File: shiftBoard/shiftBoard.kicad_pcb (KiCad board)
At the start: 2 copper layers, 88 x 93 mm, 37 parts, among them J1 Screw_Terminal_01x02, J10 Screw_Terminal_01x02, J11 Screw_Terminal_01x02, J12 Screw_Terminal_01x02, J2 Screw_Terminal_01x02, J3 Screw_Terminal_01x02, J4 Screw_Terminal_01x02, J5 Screw_Terminal_01x02, J6 Screw_Terminal_01x02, J7 Screw_Terminal_01x02, J8 Screw_Terminal_01x02, J9 Screw_Terminal_01x02, Q1 AO3400A, Q2 AO3400A, Q3 AO3400A, Q4 AO3400A, Q5 AO3400A, Q6 AO3400A, Q7 AO3400A, Q8 AO3400A, U2 74HC595

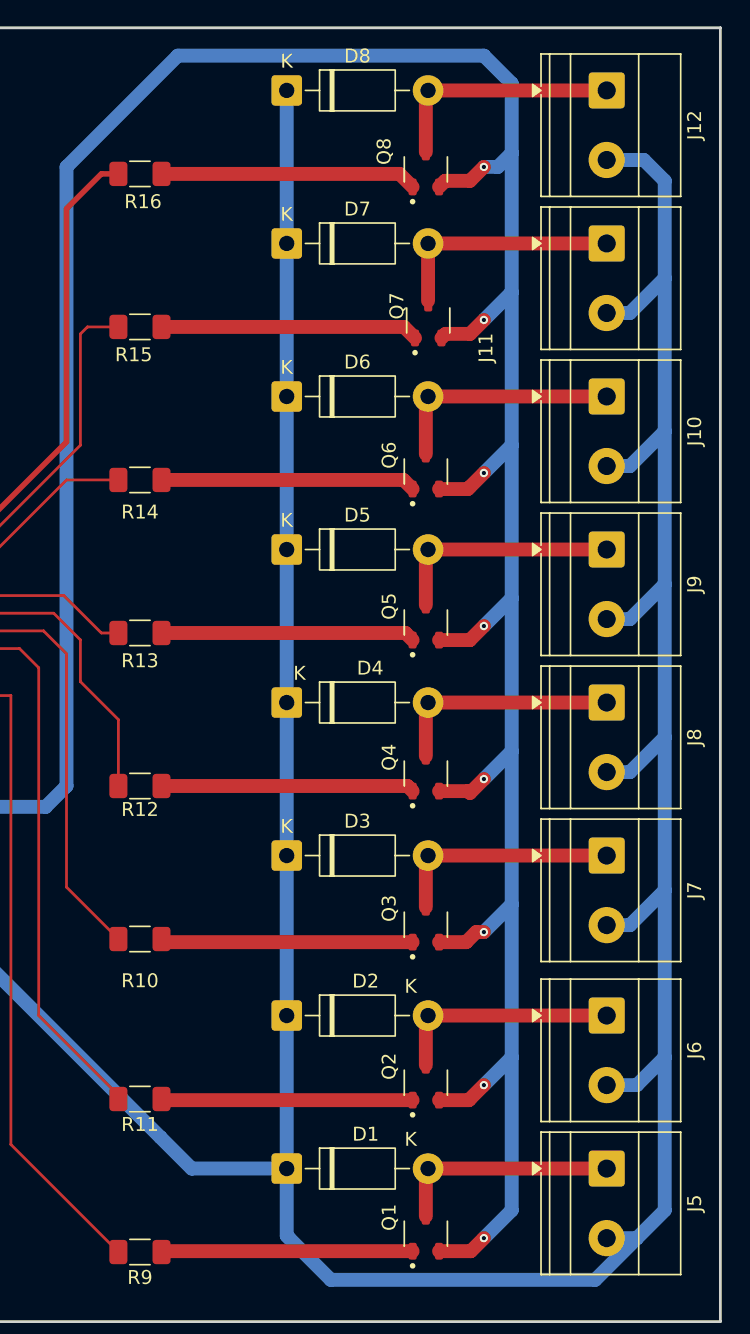
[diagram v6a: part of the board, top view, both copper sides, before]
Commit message: pcb led indicator addition
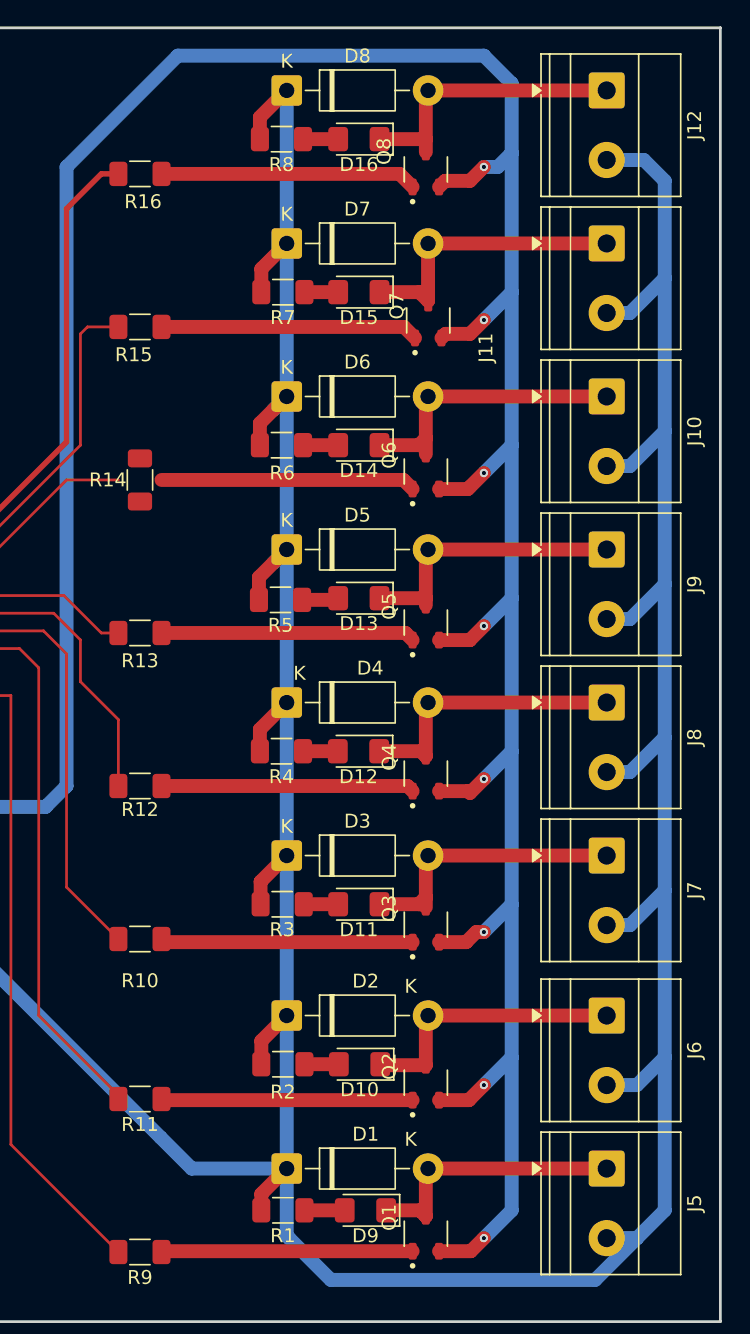
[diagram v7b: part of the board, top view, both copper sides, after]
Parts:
- added D10: LED, LED_SMD:LED_1206_3216Metric_Pad1.42x1.75mm_HandSolder, F.Cu at (224.1, 111.5)
- added D11: LED, LED_SMD:LED_1206_3216Metric_Pad1.42x1.75mm_HandSolder, F.Cu at (224.0, 100.0)
- added D12: LED, LED_SMD:LED_1206_3216Metric_Pad1.42x1.75mm_HandSolder, F.Cu at (224.0, 89.0)
- added D13: LED, LED_SMD:LED_1206_3216Metric_Pad1.42x1.75mm_HandSolder, F.Cu at (224.0, 78.0)
- added D14: LED, LED_SMD:LED_1206_3216Metric_Pad1.42x1.75mm_HandSolder, F.Cu at (224.0, 67.0)
- added D15: LED, LED_SMD:LED_1206_3216Metric_Pad1.42x1.75mm_HandSolder, F.Cu at (224.0, 56.0)
- added D16: LED, LED_SMD:LED_1206_3216Metric_Pad1.42x1.75mm_HandSolder, F.Cu at (224.0, 45.0)
- added D9: LED, LED_SMD:LED_1206_3216Metric_Pad1.42x1.75mm_HandSolder, F.Cu at (224.5, 122.0)
- added R1: 1K, Resistor_SMD:R_1206_3216Metric_Pad1.30x1.75mm_HandSolder, F.Cu at (218.6, 122.0)
- added R2: 1K, Resistor_SMD:R_1206_3216Metric_Pad1.30x1.75mm_HandSolder, F.Cu at (218.6, 111.5)
- added R3: 1K, Resistor_SMD:R_1206_3216Metric_Pad1.30x1.75mm_HandSolder, F.Cu at (218.5, 100.0)
- added R4: 1K, Resistor_SMD:R_1206_3216Metric_Pad1.30x1.75mm_HandSolder, F.Cu at (218.4, 89.0)
- added R5: 1K, Resistor_SMD:R_1206_3216Metric_Pad1.30x1.75mm_HandSolder, F.Cu at (218.4, 78.1)
- added R6: 1K, Resistor_SMD:R_1206_3216Metric_Pad1.30x1.75mm_HandSolder, F.Cu at (218.4, 67.0)
- added R7: 1K, Resistor_SMD:R_1206_3216Metric_Pad1.30x1.75mm_HandSolder, F.Cu at (218.6, 56.0)
- added R8: 1K, Resistor_SMD:R_1206_3216Metric_Pad1.30x1.75mm_HandSolder, F.Cu at (218.4, 45.0)
- turned R14 to 90 degrees
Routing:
- net /12v: track 286.0 -> 322.7 mm
- net Net-(D15-K): track 17.0 -> 20.7 mm
- net Net-(D14-K): track 17.0 -> 20.6 mm
- net Net-(D11-K): track 16.6 -> 20.2 mm
- net Net-(D12-K): track 16.8 -> 20.3 mm
- net Net-(D16-K): track 17.3 -> 20.7 mm
- net Net-(D13-K): track 16.9 -> 20.2 mm
- net Net-(D10-K): track 16.5 -> 19.8 mm
- net Net-(D1-A): track 16.3 -> 19.4 mm
- net Net-(D9-A): track 0.00 -> 2.90 mm
- net Net-(D13-A): track 0.00 -> 2.64 mm
- net Net-(D16-A): track 0.00 -> 2.53 mm
- net Net-(D14-A): track 0.00 -> 2.53 mm
- net Net-(D12-A): track 0.00 -> 2.50 mm
- net Net-(D11-A): track 0.00 -> 2.47 mm
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
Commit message: bypass capacitor
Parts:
- added C1: 100nF, Capacitor_SMD:C_1206_3216Metric_Pad1.33x1.80mm_HandSolder, F.Cu at (183.9, 58.5)
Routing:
- net /VCC: track 41.8 -> 53.1 mm
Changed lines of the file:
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@@
 		)
 	)
+	(footprint "Capacitor_SMD:C_1206_3216Metric_Pad1.33x1.80mm_HandSolder"
+		(layer "F.Cu")
+		(at 183.9375 58.5 -90)
+		(descr "Capacitor SMD 1206 (3216 Metric), square (rectangular) end terminal, IPC-7351 nominal with elongated pad for handsoldering. (Body size source: IPC-SM-782 page 76, https://www.pcb-3d.com/wordpress/wp-content/uploads/ipc-sm-782a_amendment_1_and_2.pdf), generated with kicad-footprint-generator")
+		(tags "capacitor handsolder")
+		(property "Reference" "C1"
+			(at 0 -1.85 90)
+			(layer "F.SilkS")
+			(effects
+				(font
+					(size 1 1)
+					(thickness 0.15)
+				)
+			)
+		)
+		(property "Value" "100nF"
+			(at 0 1.85 90)
+			(layer "F.Fab")
+			(effects
+				(font
+					(size 1 1)
+					(thickness 0.15)
+				)
+			)
+		)
+		(property "Datasheet" "~"
+			(at 0 0 90)
+			(layer "F.Fab")
+			(hide yes)
+			(effects
+				(font
+					(size 1.27 1.27)
+					(thickness 0.15)
+				)
+			)
+		)
+		(property "Description" "Unpolarized capacitor"
+			(at 0 0 90)
+			(layer "F.Fab")
+			(hide yes)
+			(effects
+				(font
+					(size 1.27 1.27)
+					(thickness 0.15)
+				)
+			)
+		)
+		(property ki_fp_filters "C_*")
+		(sheetname "/")
+		(sheetfile "shiftBoard.kicad_sch")
+		(attr smd)
+		(fp_line
+			(start -0.711252 0.91)
+			(end 0.711252 0.91)
+			(stroke
+				(width 0.12)
+				(type solid)
+			)
+			(layer "F.SilkS")
+		)
+		(fp_line
+			(start -0.711252 -0.91)
+			(end 0.711252 -0.91)
+			(stroke
+				(width 0.12)
+				(type solid)
+			)
+			(layer "F.SilkS")
+		)
+		(fp_rect
+			(start -2.48 -1.15)
+			(end 2.48 1.15)
+			(stroke
+				(width 0.05)
+				(type solid)
+			)
+			(fill no)
+			(layer "F.CrtYd")
+		)
+		(fp_rect
+			(start -1.6 -0.8)
+			(end 1.6 0.8)
+			(stroke
+				(width 0.1)
+				(type solid)
+			)
+			(fill no)
+			(layer "F.Fab")
+		)
+		(fp_text user "${REFERENCE}"
+			(at 0 0 90)
+			(layer "F.Fab")
+			(effects
+				(font
+					(size 0.8 0.8)
+					(thickness 0.12)
+				)
+			)
+		)
+		(pad "1" smd roundrect
+			(at -1.5625 0 270)
+			(size 1.325 1.8)
+			(layers "F.Cu" "F.Mask" "F.Paste")
+			(roundrect_rratio 0.188679)
+			(net 2 "/VCC")
+			(pintype "passive")
+		)
+		(pad "2" smd roundrect
+			(at 1.5625 0 270)
+			(size 1.325 1.8)
+			(layers "F.Cu" "F.Mask" "F.Paste")
+			(roundrect_rratio 0.188679)
+			(net 2 "/VCC")
+			(pintype "passive")
+		)
+		(embedded_fonts no)
+		(model "${KICAD9_3DMODEL_DIR}/Capacitor_SMD.3dshapes/C_1206_3216Metric.step"
+			(offset
+				(xyz 0 0 0)
+			)
+			(scale
+				(xyz 1 1 1)
+			)
+			(rotate
+				(xyz 0 0 0)
+			)
+		)
+	)
 	(footprint "Library:AO3400A"
 		(layer "F.Cu")
@@
 	)
 	(segment
+		(start 179.1675 56.9375)
+		(end 178.0525 58.0525)
+		(width 0.2)
+		(layer "F.Cu")
+		(net 2)
+	)
+	(segment
+		(start 183.9375 60.0625)
+		(end 179.0625 60.0625)
+		(width 0.2)
+		(layer "F.Cu")
+		(net 2)
+	)
+	(segment
 		(start 193 80)
 		(end 193 75)
@@
 	)
 	(segment
+		(start 179 60)
+		(end 179 59)
+		(width 0.2)
+		(layer "F.Cu")
+		(net 2)
+	)
+	(segment
+		(start 179.0625 60.0625)
+		(end 179 60)
+		(width 0.2)
+		(layer "F.Cu")
+		(net 2)
+	)
+	(segment
+		(start 183.9375 56.9375)
+		(end 179.1675 56.9375)
+		(width 0.2)
+		(layer "F.Cu")
+		(net 2)
+	)
+	(segment
 		(start 190 81.62)
 		(end 191.38 81.62)
@@
 	(segment
 		(start 179 67)
-		(end 179 59)
+		(end 179 60)
 		(width 0.2)
 		(layer "F.Cu")
